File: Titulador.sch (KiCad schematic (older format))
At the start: 29 parts, among them J1 Conn_01x02_Female, J10 Conn_01x08_Female, J11 Conn_01x08_Female, J2 Conn_01x06_Female, J3 Conn_01x04_Female, J4 Conn_01x02_Female, J5 Conn_01x08_Female, J6 Conn_01x02_Female, J7 Conn_01x05_Female, J8 Conn_01x06_Female, J9 Conn_01x06_Female, Q1 BC548, SW1 SW_DIP_x03, U1 ESP32-DEVKITC-32D

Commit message: Para correccion de companiero
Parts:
- removed J10, J11, J5: Conn_01x08_Female, symbol Connector:Conn_01x08_Female
- removed J7: Conn_01x05_Female, symbol Connector:Conn_01x05_Female
- removed J8, J9: Conn_01x06_Female, symbol Connector:Conn_01x06_Female
- added J5: 1x5_F, symbol Connector:Conn_01x05_Female
- added J7: 1x4_F, symbol Connector:Conn_01x04_Female
- added R12: 18K, symbol Device:R
- added R13: 27K, symbol Device:R
- added U2: MCU_Friend, symbol MCU_Friend:MCU_Friend
- J1, J4, J6: value Conn_01x02_Female -> 1x2_F
- J2: value Conn_01x06_Female -> 1x6_F
- J3: value Conn_01x04_Female -> 1x4_F
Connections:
- net labels added: +3.3V, +5V, Agitador, DirPAP, HCLK, HCSO, HMISO, HMOSI, StepPAP, VCLK, VCSO, VMISO, VMOSI
- wire segments 244 -> 185
- no-connect marks 28 -> 20
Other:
- note removed: "3.3V"
- note removed: "5V"
- note removed: "CS"
- note removed: "D0"
- note removed: "D1"
- note removed: "D2"
- note removed: "D3"
- note removed: "D4"
- note removed: "D5"
- note removed: "D6"
- note removed: "D7"
- note removed: "DI"
- note removed: "DO"
- note removed: "GND"
- note removed: "RD"
- note removed: "RS"
- note removed: "RST"
- note removed: "SCK"
- note removed: "SS"
- note removed: "WR"
- moved on the sheet: A1, A2, C1, D1, J1, J2, J3, J4, J6, Q1, R1, R10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

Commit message: Se agrega pcb
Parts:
- removed SW1: SW_DIP_x03, symbol Switch:SW_DIP_x03
- added SW1: SW_DIP_x04, Button_Switch_THT:SW_DIP_SPSTx04_Slide_6.7x11.72mm_W7.62mm_P2.54mm_LowProfile, symbol Switch:SW_DIP_x04
- C1: footprint (none) -> Capacitor_THT:CP_Radial_D7.5mm_P2.50mm
- D1: footprint (none) -> Diode_THT:D_A-405_P7.62mm_Horizontal
- J1, J4, J6: footprint (none) -> Connector_PinSocket_2.54mm:PinSocket_1x02_P2.54mm_Vertical
- J2: footprint (none) -> Connector_PinSocket_2.54mm:PinSocket_1x06_P2.54mm_Vertical
- J3, J7: footprint (none) -> Connector_PinSocket_2.54mm:PinSocket_1x04_P2.54mm_Vertical
- J5: footprint (none) -> Connector_PinSocket_2.54mm:PinSocket_1x05_P2.54mm_Vertical
- Q1: footprint Package_TO_SOT_THT:TO-92_Inline -> Package_TO_SOT_THT:TO-92L_HandSolder
- R1, R10, R11, R12, R13, R2, R3, R4, R5, R6, R7, R8, R9: footprint (none) -> Resistor_THT:R_Axial_DIN0207_L6.3mm_D2.5mm_P7.62mm_Horizontal
- U1: footprint MODULE_ESP32-DEVKITC-32D -> pcbTitulador:MODULE_ESP32-DEVKITC-32D; symbol ESP32-DEVKITC-32D:ESP32-DEVKITC-32D -> Titulador-rescue:ESP32-DEVKITC-32D-ESP32-DEVKITC-32D
- U2: footprint (none) -> pcbTitulador:MCUFriend; symbol MCU_Friend:MCU_Friend -> Titulador-rescue:MCU_Friend-MCU_Friend
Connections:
- no-connect marks 20 -> 22
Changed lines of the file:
@@
 $EndDescr
 $Comp
-L ESP32-DEVKITC-32D:ESP32-DEVKITC-32D U1
+L Titulador-rescue:ESP32-DEVKITC-32D-ESP32-DEVKITC-32D U1
 U 1 1 5F56BE4D
 P 4700 3850
 F 0 "U1" H 4700 5017 50  0000 C CNN
 F 1 "ESP32-DEVKITC-32D" H 4700 4926 50  0000 C CNN
-F 2 "MODULE_ESP32-DEVKITC-32D" H 4700 3850 50  0001 L BNN
+F 2 "pcbTitulador:MODULE_ESP32-DEVKITC-32D" H 4700 3850 50  0001 L BNN
 F 3 "4" H 4700 3850 50  0001 L BNN
 F 4 "Espressif Systems" H 4700 3850 50  0001 L BNN "Field4"
@@
 F 0 "R2" V 2265 2850 50  0000 C CNN
 F 1 "18K" V 2356 2850 50  0000 C CNN
-F 2 "" V 2080 2850 50  0001 C CNN
+F 2 "Resistor_THT:R_Axial_DIN0207_L6.3mm_D2.5mm_P7.62mm_Horizontal" V 2080 2850 50  0001 C CNN
 F 3 "~" H 2150 2850 50  0001 C CNN
 	1    2150 2850
@@
 F 0 "R5" H 2720 3096 50  0000 L CNN
 F 1 "27K" H 2720 3005 50  0000 L CNN
-F 2 "" V 2580 3050 50  0001 C CNN
+F 2 "Resistor_THT:R_Axial_DIN0207_L6.3mm_D2.5mm_P7.62mm_Horizontal" V 2580 3050 50  0001 C CNN
 F 3 "~" H 2650 3050 50  0001 C CNN
 	1    2650 3050
@@
 F 0 "R9" V 4793 6800 50  0000 C CNN
 F 1 "10K" V 4884 6800 50  0000 C CNN
-F 2 "" V 4930 6800 50  0001 C CNN
+F 2 "Resistor_THT:R_Axial_DIN0207_L6.3mm_D2.5mm_P7.62mm_Horizontal" V 4930 6800 50  0001 C CNN
 F 3 "~" H 5000 6800 50  0001 C CNN
 	1    5000 6800
@@
 F 0 "R10" H 2420 4496 50  0000 L CNN
 F 1 "27K" H 2420 4405 50  0000 L CNN
-F 2 "" V 2280 4450 50  0001 C CNN
+F 2 "Resistor_THT:R_Axial_DIN0207_L6.3mm_D2.5mm_P7.62mm_Horizontal" V 2280 4450 50  0001 C CNN
 F 3 "~" H 2350 4450 50  0001 C CNN
 	1    2350 4450
@@
 F 0 "R11" V 2815 4150 50  0000 C CNN
 F 1 "18K" V 2906 4150 50  0000 C CNN
-F 2 "" V 2630 4150 50  0001 C CNN
+F 2 "Resistor_THT:R_Axial_DIN0207_L6.3mm_D2.5mm_P7.62mm_Horizontal" V 2630 4150 50  0001 C CNN
 F 3 "~" H 2700 4150 50  0001 C CNN
 	1    2700 4150
@@
 F 0 "R7" H 3020 3096 50  0000 L CNN
 F 1 "27K" H 3020 3005 50  0000 L CNN
-F 2 "" V 2880 3050 50  0001 C CNN
+F 2 "Resistor_THT:R_Axial_DIN0207_L6.3mm_D2.5mm_P7.62mm_Horizontal" V 2880 3050 50  0001 C CNN
 F 3 "~" H 2950 3050 50  0001 C CNN
 	1    2950 3050
@@
 F 0 "D1" V 5550 6150 50  0000 C CNN
 F 1 "1N4007" V 5650 6050 50  0000 C CNN
-F 2 "" H 5600 6300 50  0001 C CNN
+F 2 "Diode_THT:D_A-405_P7.62mm_Horizontal" H 5600 6300 50  0001 C CNN
 F 3 "~" H 5600 6300 50  0001 C CNN
 	1    5600 6300
@@
 F 0 "Q1" H 5691 6846 50  0000 L CNN
 F 1 "BC548" H 5691 6755 50  0000 L CNN
-F 2 "Package_TO_SOT_THT:TO-92_Inline" H 5700 6725 50  0001 L CIN
+F 2 "Package_TO_SOT_THT:TO-92L_HandSolder" H 5700 6725 50  0001 L CIN
 F 3 "http://www.fairchildsemi.com/ds/BC/BC547.pdf" H 5500 6800 50  0001 L CNN
 	1    5500 6800
@@
 F 0 "J2" H 1292 2935 50  0000 C CNN
 F 1 "1x6_F" H 1292 2844 50  0000 C CNN
-F 2 "" H 1400 2550 50  0001 C CNN
+F 2 "Connector_PinSocket_2.54mm:PinSocket_1x06_P2.54mm_Vertical" H 1400 2550 50  0001 C CNN
 F 3 "~" H 1400 2550 50  0001 C CNN
 	1    1400 2550
@@
 F 0 "J3" H 3442 6225 50  0000 C CNN
 F 1 "1x4_F" H 3442 6316 50  0000 C CNN
-F 2 "" H 3550 6650 50  0001 C CNN
+F 2 "Connector_PinSocket_2.54mm:PinSocket_1x04_P2.54mm_Vertical" H 3550 6650 50  0001 C CNN
 F 3 "~" H 3550 6650 50  0001 C CNN
 	1    3550 6650
@@
 F 0 "C1" H 1618 5996 50  0000 L CNN
 F 1 "100uF" H 1618 5905 50  0000 L CNN
-F 2 "" H 1538 5800 50  0001 C CNN
+F 2 "Capacitor_THT:CP_Radial_D7.5mm_P2.50mm" H 1538 5800 50  0001 C CNN
 F 3 "~" H 1500 5950 50  0001 C CNN
 	1    1500 5950
 	-1   0    0    -1
-$EndComp
-$Comp
-L Switch:SW_DIP_x03 SW1
-U 1 1 5F57DE7B
-P 1350 7100
-F 0 "SW1" H 1350 6925 50  0000 C CNN
-F 1 "SW_DIP_x03" H 1350 6834 50  0000 C CNN
-F 2 "" H 1350 7100 50  0001 C CNN
-F 3 "~" H 1350 7100 50  0001 C CNN
-	1    1350 7100
-	1    0    0    -1
 $EndComp
 $Comp
@@
 F 0 "J4" H 1192 1235 50  0000 C CNN
 F 1 "1x2_F" H 1350 1150 50  0000 C CNN
-F 2 "" H 1300 1050 50  0001 C CNN
+F 2 "Connector_PinSocket_2.54mm:PinSocket_1x02_P2.54mm_Vertical" H 1300 1050 50  0001 C CNN
 F 3 "~" H 1300 1050 50  0001 C CNN
 	1    1300 1050
@@
 F 0 "J6" H 6300 6500 50  0000 L CNN
 F 1 "1x2_F" H 6100 6200 50  0000 L CNN
-F 2 "" H 6400 6350 50  0001 C CNN
+F 2 "Connector_PinSocket_2.54mm:PinSocket_1x02_P2.54mm_Vertical" H 6400 6350 50  0001 C CNN
 F 3 "~" H 6400 6350 50  0001 C CNN
 	1    6400 6350
@@
 F 0 "R1" V 1943 2650 50  0000 C CNN
 F 1 "18K" V 2034 2650 50  0000 C CNN
-F 2 "" V 2080 2650 50  0001 C CNN
+F 2 "Resistor_THT:R_Axial_DIN0207_L6.3mm_D2.5mm_P7.62mm_Horizontal" V 2080 2650 50  0001 C CNN
 F 3 "~" H 2150 2650 50  0001 C CNN
 	1    2150 2650
@@
 F 0 "J1" H 1242 1935 50  0000 C CNN
 F 1 "1x2_F" H 1242 1844 50  0000 C CNN
-F 2 "" H 1350 1750 50  0001 C CNN
+F 2 "Connector_PinSocket_2.54mm:PinSocket_1x02_P2.54mm_Vertical" H 1350 1750 50  0001 C CNN
 F 3 "~" H 1350 1750 50  0001 C CNN
 	1    1350 1750
@@
 F 0 "R6" V 2915 1850 50  0000 C CNN
 F 1 "18K" V 3006 1850 50  0000 C CNN
-F 2 "" V 2730 1850 50  0001 C CNN
+F 2 "Resistor_THT:R_Axial_DIN0207_L6.3mm_D2.5mm_P7.62mm_Horizontal" V 2730 1850 50  0001 C CNN
 F 3 "~" H 2800 1850 50  0001 C CNN
 	1    2800 1850
@@
 F 0 "R3" V 2043 1750 50  0000 C CNN
 F 1 "18K" V 2134 1750 50  0000 C CNN
-F 2 "" V 2180 1750 50  0001 C CNN
+F 2 "Resistor_THT:R_Axial_DIN0207_L6.3mm_D2.5mm_P7.62mm_Horizontal" V 2180 1750 50  0001 C CNN
 F 3 "~" H 2250 1750 50  0001 C CNN
 	1    2250 1750
@@
 F 0 "R8" H 3220 2146 50  0000 L CNN
 F 1 "27K" H 3220 2055 50  0000 L CNN
-F 2 "" V 3080 2100 50  0001 C CNN
+F 2 "Resistor_THT:R_Axial_DIN0207_L6.3mm_D2.5mm_P7.62mm_Horizontal" V 3080 2100 50  0001 C CNN
 F 3 "~" H 3150 2100 50  0001 C CNN
 	1    3150 2100
@@
 F 0 "R4" H 2570 2146 50  0000 L CNN
 F 1 "27K" H 2570 2055 50  0000 L CNN
-F 2 "" V 2430 2100 50  0001 C CNN
+F 2 "Resistor_THT:R_Axial_DIN0207_L6.3mm_D2.5mm_P7.62mm_Horizontal" V 2430 2100 50  0001 C CNN
 F 3 "~" H 2500 2100 50  0001 C CNN
 	1    2500 2100
@@
 	8500 3150 9800 3150
 $Comp
-L MCU_Friend:MCU_Friend U2
+L Titulador-rescue:MCU_Friend-MCU_Friend U2
 U 1 1 5F829702
 P 10200 3350
 F 0 "U2" H 10600 3200 50  0000 C CNN
 F 1 "MCU_Friend" H 10700 3400 50  0000 C CNN
-F 2 "" H 10300 3350 50  0001 C CNN
+F 2 "pcbTitulador:MCUFriend" H 10300 3350 50  0001 C CNN
 F 3 "" H 10300 3350 50  0001 C CNN
 	1    10200 3350
@@
 F 0 "J5" H 1292 4135 50  0000 C CNN
 F 1 "1x5_F" H 1292 4044 50  0000 C CNN
-F 2 "" H 1400 3750 50  0001 C CNN
+F 2 "Connector_PinSocket_2.54mm:PinSocket_1x05_P2.54mm_Vertical" H 1400 3750 50  0001 C CNN
 F 3 "~" H 1400 3750 50  0001 C CNN
 	1    1400 3750
@@
 F 0 "J7" H 5950 3950 50  0000 L CNN
 F 1 "1x4_F" H 5900 3850 50  0000 L CNN
-F 2 "" H 5900 4150 50  0001 C CNN
+F 2 "Connector_PinSocket_2.54mm:PinSocket_1x04_P2.54mm_Vertical" H 5900 4150 50  0001 C CNN
 F 3 "~" H 5900 4150 50  0001 C CNN
 	1    5900 4150
@@
 F 0 "R13" H 6370 3846 50  0000 L CNN
 F 1 "27K" H 6370 3755 50  0000 L CNN
-F 2 "" V 6230 3800 50  0001 C CNN
+F 2 "Resistor_THT:R_Axial_DIN0207_L6.3mm_D2.5mm_P7.62mm_Horizontal" V 6230 3800 50  0001 C CNN
 F 3 "~" H 6300 3800 50  0001 C CNN
 	1    6300 3800
@@
 F 0 "R12" V 5643 3650 50  0000 C CNN
 F 1 "18K" V 5734 3650 50  0000 C CNN
-F 2 "" V 5780 3650 50  0001 C CNN
+F 2 "Resistor_THT:R_Axial_DIN0207_L6.3mm_D2.5mm_P7.62mm_Horizontal" V 5780 3650 50  0001 C CNN
 F 3 "~" H 5850 3650 50  0001 C CNN
 	1    5850 3650
@@
 Wire Wire Line
 	5600 7000 5600 7200
+$Comp
+L Switch:SW_DIP_x04 SW1
+U 1 1 5F92A150
+P 1350 7100
+F 0 "SW1" H 1350 7567 50  0000 C CNN
+F 1 "SW_DIP_x04" H 1350 7476 50  0000 C CNN
+F 2 "Button_Switch_THT:SW_DIP_SPSTx04_Slide_6.7x11.72mm_W7.62mm_P2.54mm_LowProfile" H 1350 7100 50  0001 C CNN
+F 3 "~" H 1350 7100 50  0001 C CNN
+	1    1350 7100
+	1    0    0    -1
+$EndComp
+NoConn ~ 1050 7200
+NoConn ~ 1650 7200
 $EndSCHEMATC

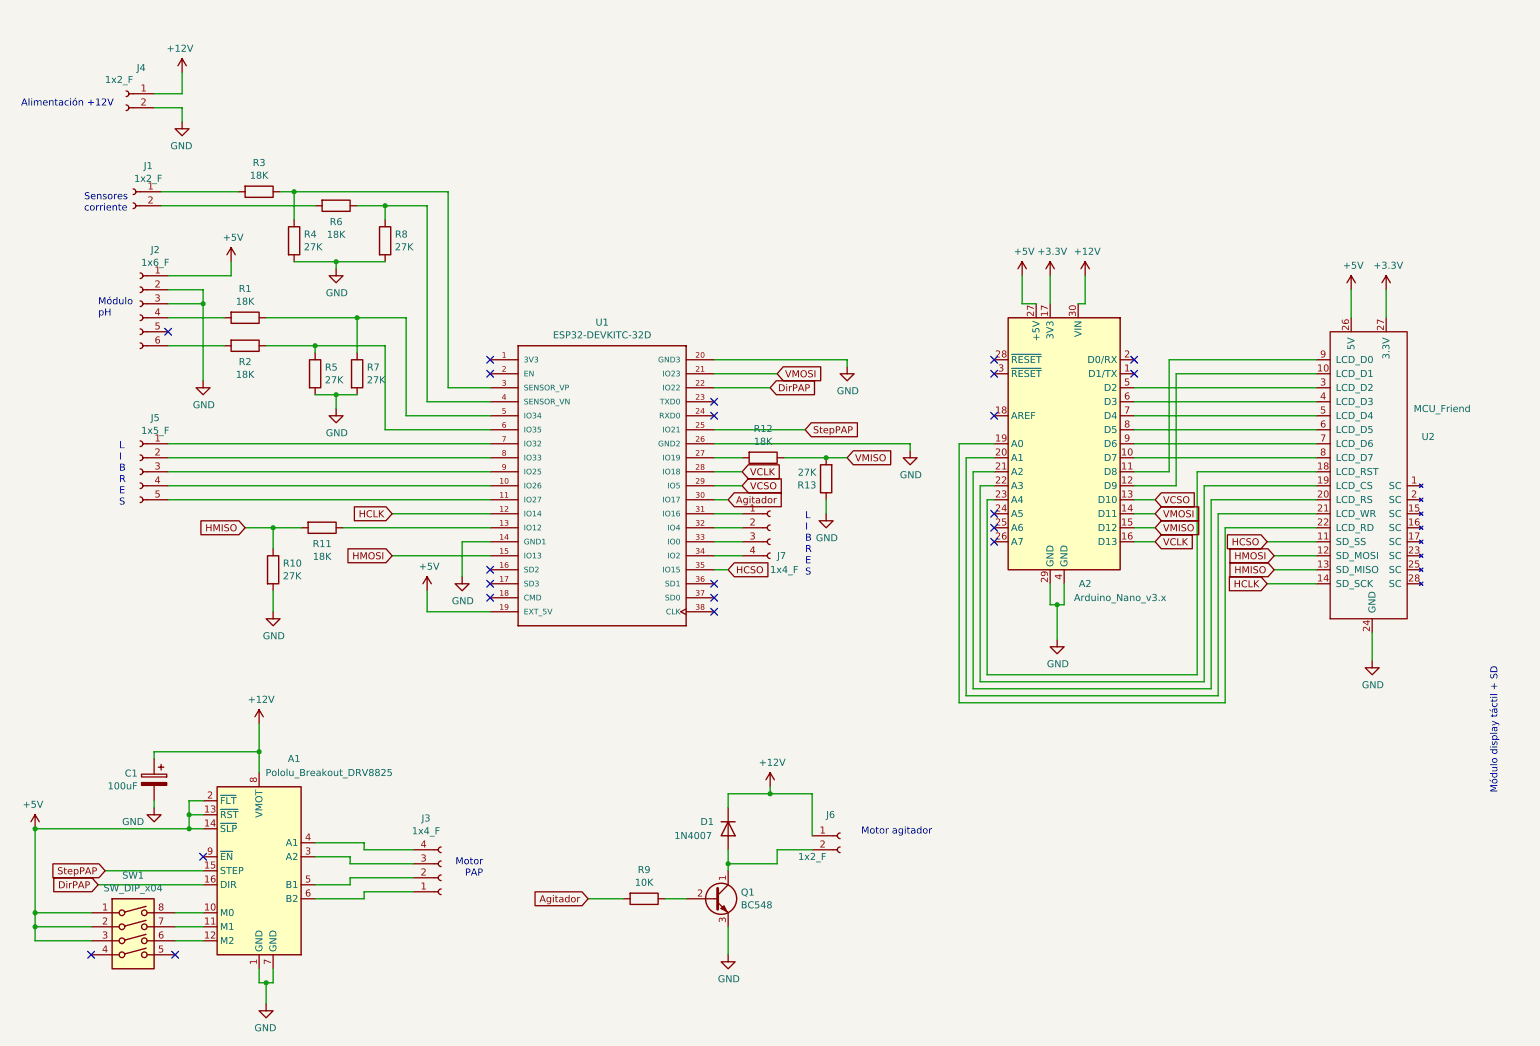
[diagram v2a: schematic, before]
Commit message: Se actualiza esquematico con atmega328pu
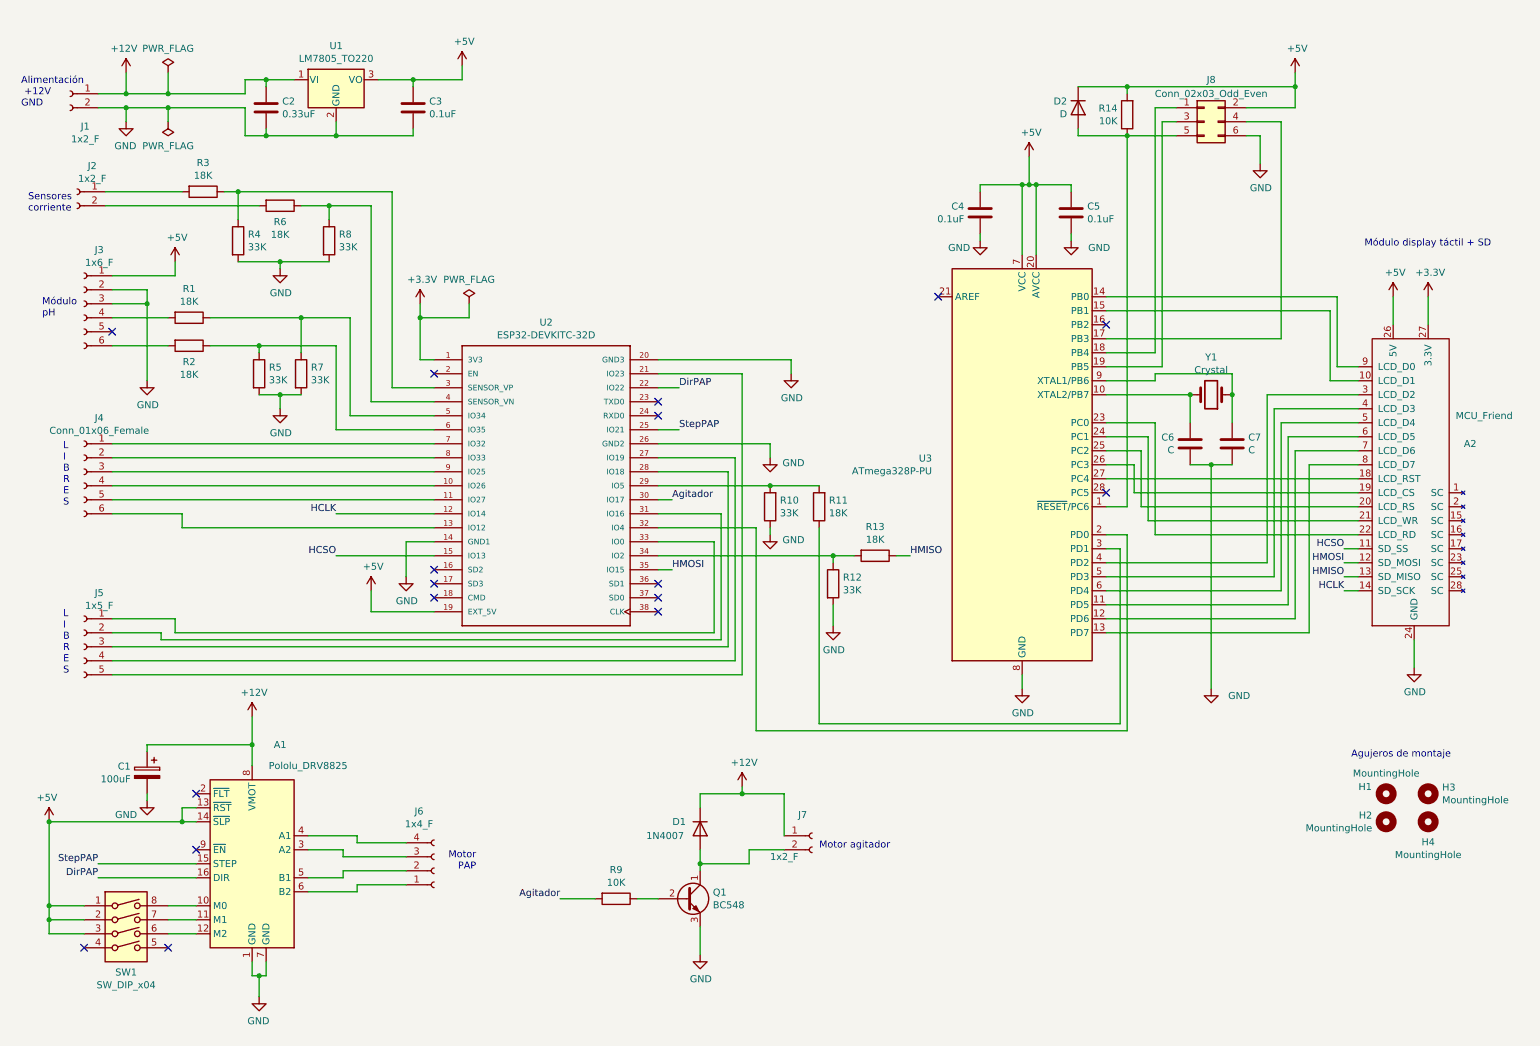
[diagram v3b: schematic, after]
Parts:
- removed A2: Arduino_Nano_v3.x, Module:Arduino_Nano, symbol MCU_Module:Arduino_Nano_v3.x
- removed J7: 1x4_F, Connector_PinSocket_2.54mm:PinSocket_1x04_P2.54mm_Vertical, symbol Connector:Conn_01x04_Female
- added C2: 0.33uF, symbol Device:C
- added C3, C4, C5: 0.1uF, symbol Device:C
- added C6, C7: C, symbol Device:C
- added D2: D, symbol Device:D
- added H1, H2, H3, H4: MountingHole, MountingHole:MountingHole_3mm, symbol Mechanical:MountingHole
- added J4: Conn_01x06_Female, symbol Connector:Conn_01x06_Female
- added J8: Conn_02x03_Odd_Even, symbol Connector_Generic:Conn_02x03_Odd_Even
- added R14: 10K, Resistor_THT:R_Axial_DIN0207_L6.3mm_D2.5mm_P7.62mm_Horizontal, symbol Device:R
- added U1: LM7805_TO220, Package_TO_SOT_THT:TO-220-3_Vertical, symbol Regulator_Linear:LM7805_TO220
- added U3: ATmega328P-PU, Package_DIP:DIP-28_W7.62mm, symbol MCU_Microchip_ATmega:ATmega328P-PU
- added Y1: Crystal, symbol Device:Crystal
- A1: value Pololu_Breakout_DRV8825 -> Pololu_DRV8825
- Q1: footprint Package_TO_SOT_THT:TO-92L_HandSolder -> Package_TO_SOT_THT:TO-92L_Wide
- R10: renamed from R13; value 27K -> 33K
- R12: renamed from R10; value 27K -> 33K
- R4, R5, R7, R8: value 27K -> 33K
- renumbered U2 to A2, J4 to J1, J1 to J2, J2 to J3, J3 to J6, J6 to J7, R12 to R11, R11 to R13, U1 to U2
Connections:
- net VCLK is gone; now on an unnamed net: U2.28 (IO18)
- net +12V: now also C2.1, U1.1 (VI)
- net +3V3: now also U2.1 (3V3)
- net +5V: now also C3.1, C4.1, C5.1, D2.1 (K), J8.2 (Pin_2), R14.2, U1.3 (VO), U3.20 (AVCC), U3.7 (VCC); no longer A1.2 (~FLT)
- net GND: now also C2.2, C3.2, C4.2, C5.2, C6.1, C7.2, J8.6 (Pin_6), U1.2 (GND), U3.22 (GND), U3.8 (GND)
- net HCSO: now also U2.15 (IO13); no longer U2.35 (IO15)
- net HMISO: now also R13.1; no longer R12.1, R13.2
- net HMOSI: now also U2.35 (IO15); no longer U2.15 (IO13)
- net at U2.10 (IO26): now also J4.4 (Pin_4); no longer J5.4 (Pin_4)
- net at U2.11 (IO27): now also J4.5 (Pin_5); no longer J5.5 (Pin_5)
- net at U2.13 (IO12): now also J4.6 (Pin_6); no longer R13.1
- net at U2.27 (IO19): now also J5.4 (Pin_4); no longer R11.2
- net at U2.31 (IO16): now also J5.2 (Pin_2)
- net at U2.32 (IO4): now also U3.2 (PD0)
- net at U2.33 (IO0): now also J5.1 (Pin_1)
- net at U2.34 (IO2): now also R12.1, R13.2
- net at U2.7 (IO32): now also J4.1 (Pin_1); no longer J5.1 (Pin_1)
- net at U2.8 (IO33): now also J4.2 (Pin_2); no longer J5.2 (Pin_2)
- net at J5.3 (Pin_3): no longer U2.9 (IO25)
- net at A2.8 (LCD_D7): now also U3.13 (PD7)
- net at A2.9 (LCD_D0): now also U3.14 (PB0)
- net at A2.10 (LCD_D1): now also U3.15 (PB1)
- net at A2.22 (LCD_RD): now also U3.23 (PC0)
- net at A2.21 (LCD_WR): now also U3.24 (PC1)
- net at A2.20 (LCD_RS): now also U3.25 (PC2)
- net at A2.19 (LCD_CS): now also U3.26 (PC3)
- net at A2.18 (LCD_RST): now also U3.27 (PC4)
- net at A2.3 (LCD_D2): now also U3.4 (PD2)
- net at A2.4 (LCD_D3): now also U3.5 (PD3)
- net at A2.5 (LCD_D4): now also U3.6 (PD4)
- net at A2.6 (LCD_D5): now also U3.11 (PD5)
- net at A2.7 (LCD_D6): now also U3.12 (PD6)
- net VCSO: no longer names the net of U2.29 (IO5)
- net VCSO: now also R10.2, R11.2
- net VMISO: no longer names the net of R11.1
- net VMISO: now also U3.3 (PD1); no longer R10.2
- net VMOSI: no longer names the net of U2.21 (IO23)
- net VMOSI: now also J5.5 (Pin_5)
- new net: J4.3 (Pin_3), U2.9 (IO25)
- new net: D2.2 (A), J8.5 (Pin_5), R14.1, U3.1 (~RESET~/PC6)
- new net: C6.2, U3.10 (XTAL2/PB7), Y1.2
- new net: J8.4 (Pin_4), U3.17 (PB3)
- new net: J8.1 (Pin_1), U3.18 (PB4)
- new net: J8.3 (Pin_3), U3.19 (PB5)
- new net: C7.1, U3.9 (XTAL1/PB6), Y1.1
- no-connect marks 22 -> 17
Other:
- note added: "Agujeros de montaje"
- note added: "Alimentación\n +12V\nGND"
- note removed: "Alimentación +12V"
- moved on the sheet: A1, A2, C1, D1, J1, J2, J3, J6, J7, Q1, R1, R10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
